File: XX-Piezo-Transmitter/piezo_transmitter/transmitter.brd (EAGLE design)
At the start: 26.2 x 26.4 mm, 5 parts, among them U1 BD6221FSOP, U2 ATTINY24A-SSUR

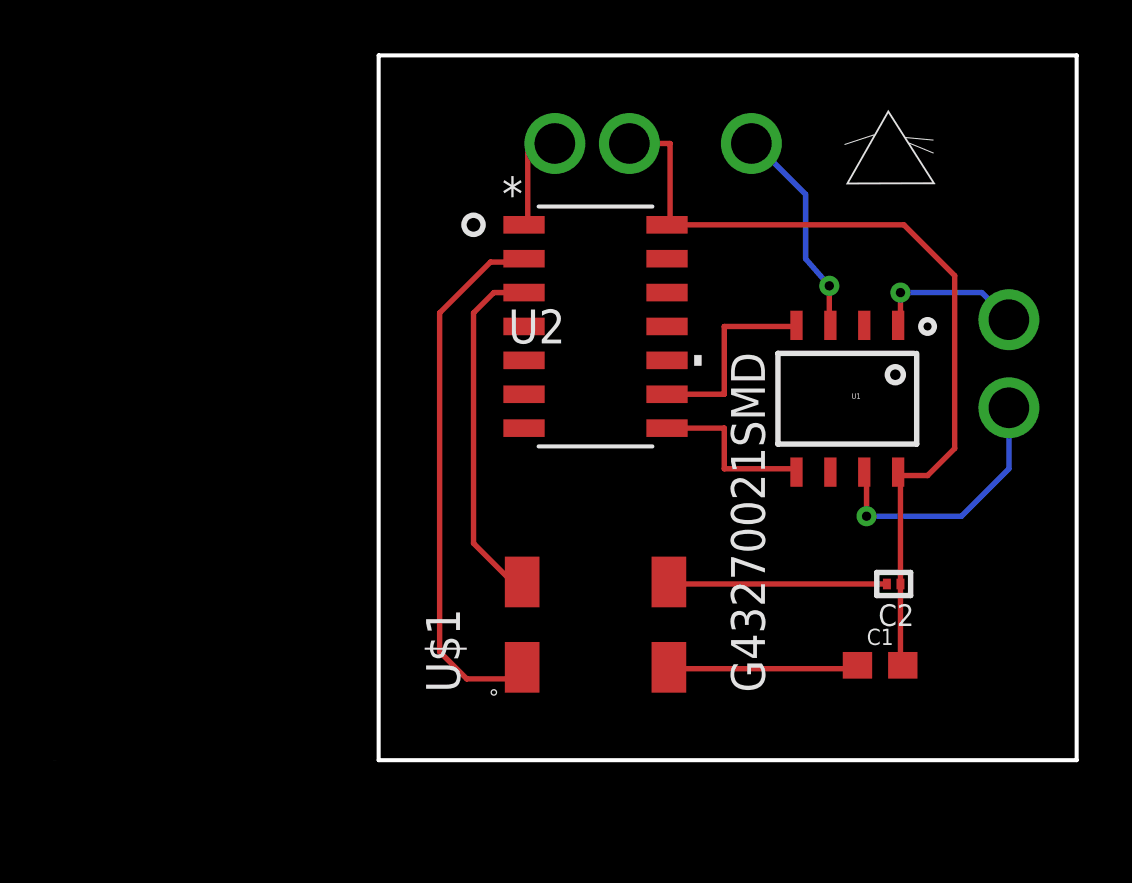
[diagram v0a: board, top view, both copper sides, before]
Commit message: Added pin headers & pwm line, crystal and caps change.
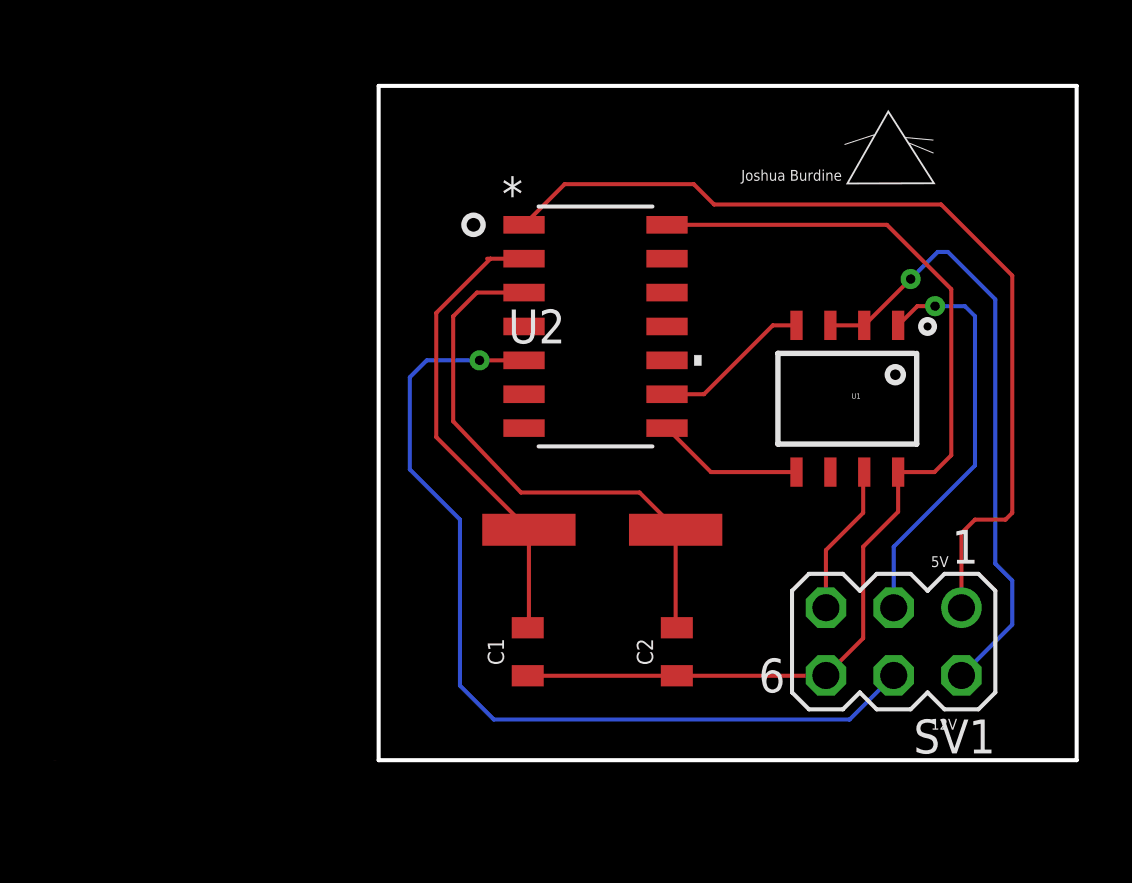
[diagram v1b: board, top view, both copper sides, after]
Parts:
- added SV1: (no value), con-lstb:MA03-2
- C1: value 16.0pF -> 22pF; device SparkFun-Capacitors:0603 -> SparkFun-Capacitors:0805
- C2: value 6.0pF -> 22pF; device rc-master-smd:C0201 -> SparkFun-Capacitors:0805
- U$1: value G43270021SMD -> ABLS7M2-16; device G43270021 Oscillator:G43270021 -> ABLS7M2-16:ABLS7M2-16
- moved C1 13.2 mm to (17.8, 4.06), turned to 90 degrees
- moved C2 8.52 mm to (23.4, 4.06), turned to 90 degrees
- moved U$1 3.57 mm to (20.6, 8.64)
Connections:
- net N$6 renamed FIN
- net N$7 renamed RIN
- removed net C1: C1.1, U$1.C1
- removed net C2: C2.2, U$1.C2
- removed net N$1: U$1.XTAL1, U2.2
- removed net N$2: U$1.XTAL2, U2.3
- removed net N$5: U2.1
- removed net N$8: U1.1
- removed net N$9: U1.7
- new net PIEZO+: SV1.3, U1.1
- new net PIEZO-: SV1.5, U1.7
- new net PWM: SV1.4, U2.5
- new net VCC_2: SV1.1, U2.1
- new net XTAL1: C1.2, U$1.P$1, U2.2
- new net XTAL2: C2.2, U$1.P$2, U2.3
- net GND: now also C1.1, SV1.6; no longer C1.2
- net VCC: now also SV1.2
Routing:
- net PWM: track 0.00 -> 34.3 mm, vias 0 -> 1
- net VCC_2: track 0.00 -> 34.3 mm
- net VCC: track 0.00 -> 23.2 mm, vias 0 -> 1
- net XTAL2: track 0.00 -> 20.7 mm
- net N$4: track 20.1 -> 0.00 mm
- net XTAL1: track 0.00 -> 17.5 mm
- net N$3: track 13.4 -> 0.00 mm
- net PIEZO+: track 5.75 -> 15.5 mm, vias 2 -> 1
- net C2: track 8.13 -> 0.00 mm
- net VCC(12): track 7.98 -> 0.00 mm, vias 2 -> 0
- net GND: track 32.2 -> 40.1 mm, vias 1 -> 0
- net N$14: track 7.37 -> 0.00 mm
- net N$12: track 7.11 -> 0.00 mm
- net N$13: track 6.35 -> 0.00 mm
- net FIN: track 0.00 -> 5.92 mm
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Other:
- board size 26.2 x 26.4 mm -> 26.2 x 25.3 mm
- board text added: "12V"
- board text added: "5V"
- board text added: "Joshua Burdine"

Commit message: Change to through hole crystal. Change to LV 22pf cap.
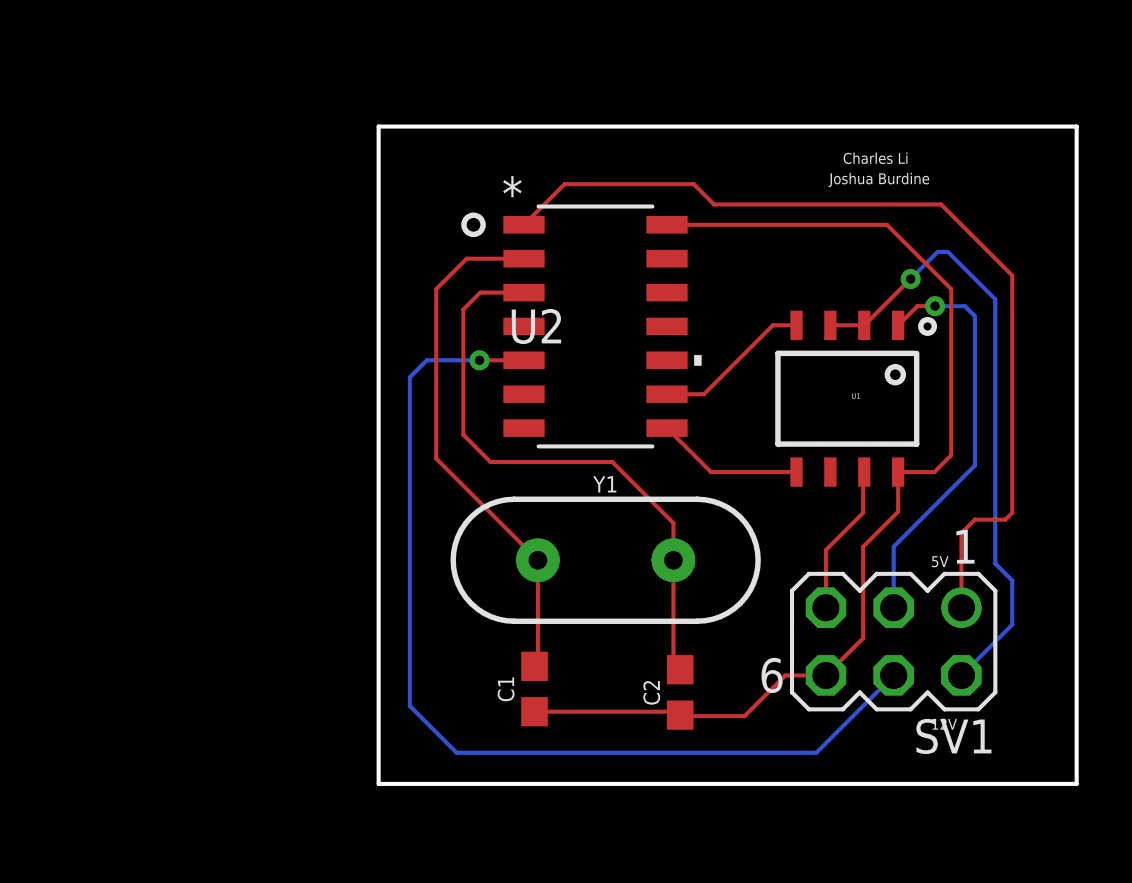
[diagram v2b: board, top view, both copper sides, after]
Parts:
- removed U$1: ABLS7M2-16, ABLS7M2-16:ABLS7M2-16
- added Y1: (no value), SparkFun-Clocks:HC49US
- C1, C2: device SparkFun-Capacitors:0805 -> SparkFun-Retired:0603
- moved C2 1.53 mm to (23.5, 2.54)
- moved C1 1.42 mm to (18.0, 2.67)
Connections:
- removed net XTAL1: C1.2, U$1.P$1, U2.2
- removed net XTAL2: C2.2, U$1.P$2, U2.3
- new net N$2: C1.2, U2.2, Y1.1
- new net N$3: C2.2, U2.3, Y1.2
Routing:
- net N$3: track 0.00 -> 22.1 mm
- net XTAL2: track 20.7 -> 0.00 mm
- net N$2: track 0.00 -> 19.5 mm
- net XTAL1: track 17.5 -> 0.00 mm
- net PWM: track 34.3 -> 36.9 mm
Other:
- board size 26.2 x 25.3 mm -> 26.2 x 24.6 mm
- board text added: "Charles Li"

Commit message: Fixed oscillator trace lengths and board trace widths. Added programmer header and mounting holes. Board about 1 squ in now.
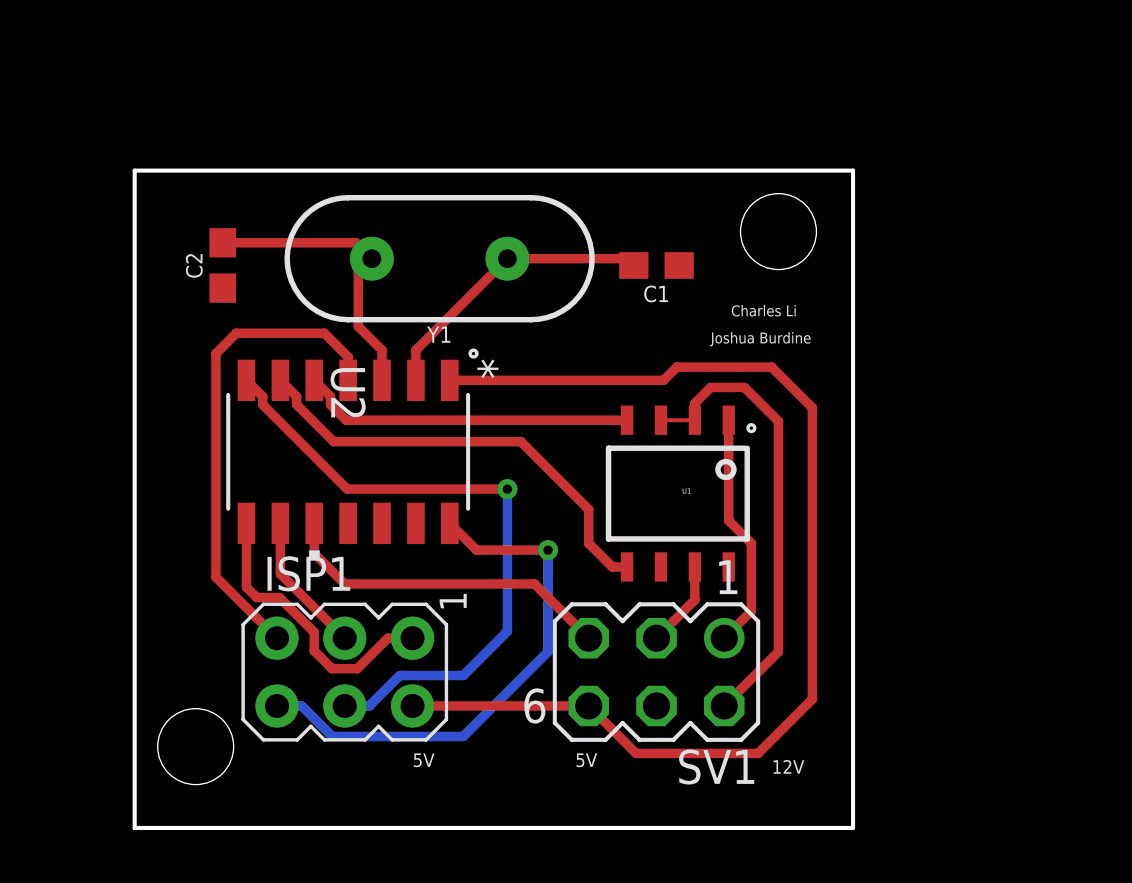
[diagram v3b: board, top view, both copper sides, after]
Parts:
- added ISP1: AVRISP-6, adafruit:AVRISP
- moved C2 23.5 mm to (6.35, 18.5)
- moved C1 16.5 mm to (22.6, 18.5), turned to 180 degrees
- moved Y1 12.9 mm to (14.5, 18.8), turned to 180 degrees
- moved U2 10.4 mm to (11.0, 11.6), turned to 270 degrees
- moved SV1 8.96 mm to (22.6, 3.30)
- moved U1 7.28 mm to (25.9, 12.2)
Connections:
- removed net FIN: U1.4, U2.9
- removed net PIEZO+: SV1.3, U1.1
- removed net PIEZO-: SV1.5, U1.7
- removed net PWM: SV1.4, U2.5
- removed net RIN: U1.5, U2.8
- new net N$10: U1.5, U2.6
- new net N$11: ISP1.3, U2.9
- new net N$12: ISP1.1, U2.8
- new net N$4: ISP1.4, U2.7
- new net N$5: SV1.5, U2.10
- new net N$6: ISP1.5, U2.4
- new net N$7: SV1.1, U1.1
- new net N$8: SV1.3, U1.7
- new net N$9: U1.4, U2.5
- net GND: now also ISP1.6, SV1.4; no longer SV1.6
- net VCC_2: now also ISP1.2, SV1.6; no longer SV1.1
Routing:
- net PWM: track 36.9 -> 0.00 mm, vias 1 -> 0
- net N$4: track 0.00 -> 24.2 mm, vias 0 -> 1
- net GND: track 40.5 -> 19.9 mm, vias 0 -> 1
- net N$6: track 0.00 -> 18.1 mm
- net N$10: track 0.00 -> 16.8 mm
- net PIEZO+: track 15.5 -> 0.00 mm, vias 1 -> 0
- net N$5: track 0.00 -> 12.7 mm
- net N$9: track 0.00 -> 12.5 mm
- net N$3: track 22.1 -> 11.0 mm
- net N$12: track 0.00 -> 10.8 mm
- net N$7: track 0.00 -> 8.94 mm
- net N$2: track 19.5 -> 11.2 mm
- net VCC_2: track 34.3 -> 41.9 mm
- net FIN: track 5.92 -> 0.00 mm
- net VCC: track 23.2 -> 17.3 mm, vias 1 -> 0
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- added copper zone on layer 1, net GND
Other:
- board size 26.2 x 24.6 mm -> 26.9 x 24.6 mm
